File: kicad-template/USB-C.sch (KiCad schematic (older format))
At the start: 4 parts

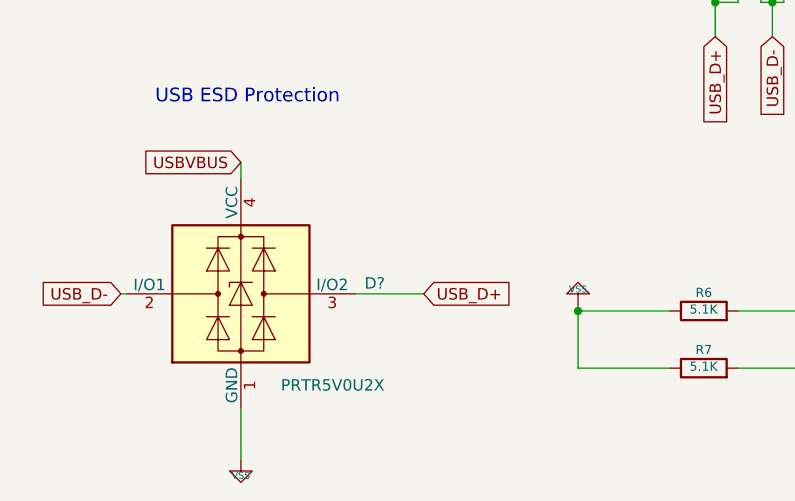
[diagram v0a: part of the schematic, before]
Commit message: working on adding support for jlcpcb small batch assembly
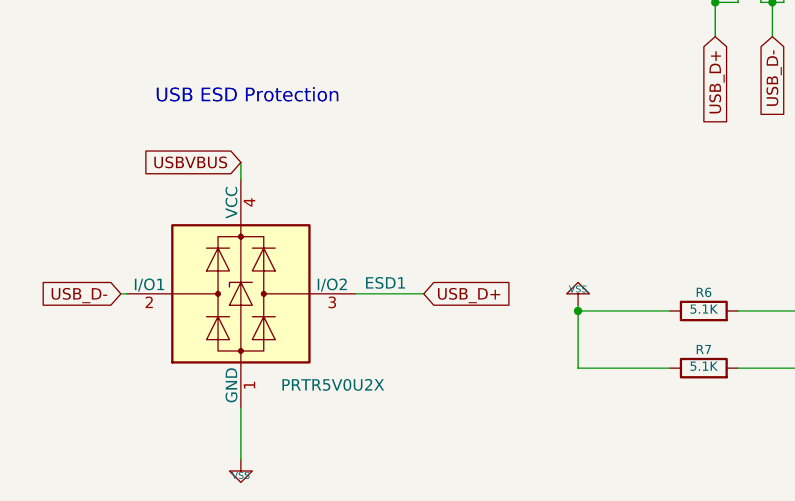
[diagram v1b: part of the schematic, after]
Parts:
- ESD1: LCSC (none) -> C12333
- R7: DigiKey RR08P5.1KDTR-ND -> YAG1696TR-ND; LCSC (none) -> C122969; MPN RR0816P-512-D -> RT0603BRD075K1L; Manufacturer Susumu -> Yaego
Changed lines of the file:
@@
 AR Path="/5B90A59F/5B5FAE80" Ref="R7"  Part="1"
 AR Path="/5D950BDF/5B5FAE80" Ref="R?"  Part="1"
-F 0 "R?" V 3980 5350 40  0000 C CNN
+F 0 "R7" V 3980 5350 40  0000 C CNN
 F 1 "5.1K" V 3907 5351 40  0000 C CNN
 F 2 "Resistor_SMD:R_0603_1608Metric" V 3830 5350 30  0001 C CNN
-F 3 "http://www.susumu.co.jp/common/pdf/n_catalog_partition05_en.pdf" H 3900 5350 30  0001 C CNN
-F 4 "RR0816P-512-D" V 3900 5350 50  0001 C CNN "MPN"
+F 3 "" H 3900 5350 30  0001 C CNN
+F 4 "RT0603BRD075K1L" V 3900 5350 50  0001 C CNN "MPN"
 F 5 "RES SMD 5.1K OHM 0.5% 1/16W 0603" H -5700 275 50  0001 C CNN "Description"
-F 6 "RR08P5.1KDTR-ND" H -5700 275 50  0001 C CNN "DigiKey"
-F 7 "Susumu" H -5700 275 50  0001 C CNN "Manufacturer"
+F 6 "YAG1696TR-ND" H -5700 275 50  0001 C CNN "DigiKey"
+F 7 "Yaego" H -5700 275 50  0001 C CNN "Manufacturer"
 F 8 "RT0603BRD075K1L	" H 0   0   50  0001 C CNN "Seeed Part Num"
+F 9 "C122969" V 3900 5350 50  0001 C CNN "LCSC"
 	1    3900 5350
 	0    -1   -1   0
@@
 AR Path="/5B90A59F/5B5FB101" Ref="R6"  Part="1"
 AR Path="/5D950BDF/5B5FB101" Ref="R?"  Part="1"
-F 0 "R?" V 3980 5100 40  0000 C CNN
+F 0 "R6" V 3980 5100 40  0000 C CNN
 F 1 "5.1K" V 3907 5101 40  0000 C CNN
 F 2 "Resistor_SMD:R_0603_1608Metric" V 3830 5100 30  0001 C CNN
@@
 AR Path="/5B90A59F/5B5FB0C4" Ref="USB1"  Part="1"
 AR Path="/5D950BDF/5B5FB0C4" Ref="USB?"  Part="1"
-F 0 "USB?" V 3809 4329 50  0000 L CNN
+F 0 "USB1" V 3809 4329 50  0000 L CNN
 F 1 "USB_C_Receptacle" V 3900 4329 50  0000 L CNN
 F 2 "Keyboardio:USB-TYPE-C-MIDMOUNT" H 3900 2900 50  0001 C CNN
@@
 AR Path="/5B90A59F/5CA6A217" Ref="ESD1"  Part="1"
 AR Path="/5D950BDF/5CA6A217" Ref="D?"  Part="1"
-F 0 "D?" H 2416 5071 50  0000 L CNN
+F 0 "ESD1" H 2416 5071 50  0000 L CNN
 F 1 "PRTR5V0U2X" H 2050 4625 50  0000 L CNN
 F 2 "Keyboardio:PRTR5V0U2X" H 1935 5025 50  0001 C CNN
@@
 F 7 "Nexperia" H -2925 -125 50  0001 C CNN "Manufacturer"
 F 8 "PRTR5V0U2X,215	" H 0   0   50  0001 C CNN "Seeed Part Num"
+F 9 "C12333" H 1875 5025 50  0001 C CNN "LCSC"
 	1    1875 5025
 	1    0    0    -1

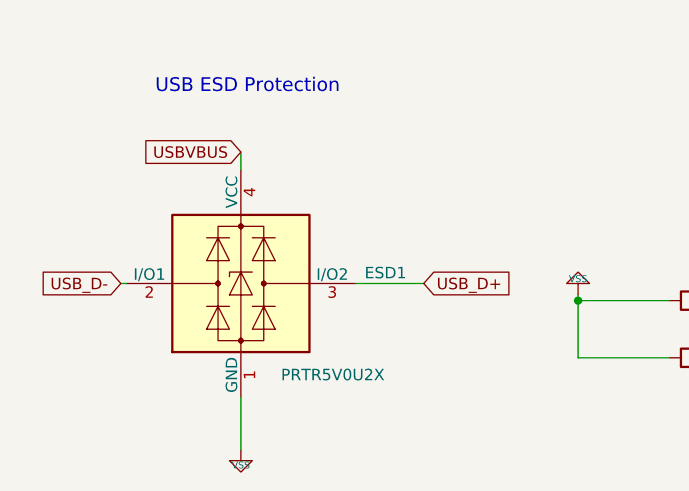
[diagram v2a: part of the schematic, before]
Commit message: Trying to get back to Kicad 5.1 compat and fix USB routing
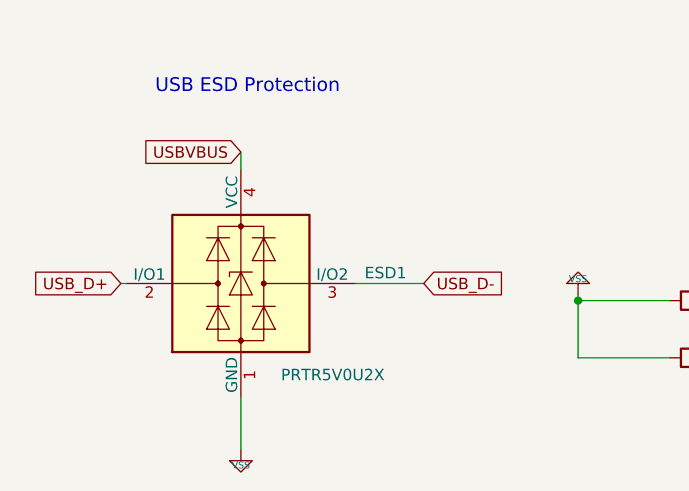
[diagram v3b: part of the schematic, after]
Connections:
- net USB_D+: now also ESD1.2 (I/O1); no longer ESD1.3 (I/O2)
- net USB_D-: now also ESD1.3 (I/O2); no longer ESD1.2 (I/O1)
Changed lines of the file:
@@
-EESchema Schematic File Version 5
+EESchema Schematic File Version 4
 LIBS:kicad-template-cache
 EELAYER 30 0
@@
 Comment3 ""
 Comment4 ""
-Comment5 ""
-Comment6 ""
-Comment7 ""
-Comment8 ""
-Comment9 ""
 $EndDescr
 $Comp
@@
 U 1 1 5CA6F860
 P 1850 2800
-AR Path="/5B90A59F/5CA6F860" Ref="#FLG?"  Part="1"
-AR Path="/5D950BDF/5CA6F860" Ref="#FLG?"  Part="1"
 F 0 "#FLG?" H 1850 2895 50  0001 C CNN
 F 1 "PWR_FLAG" V 1850 3100 50  0000 C CNN
@@
 U 1 1 5B5FAE80
 P 3900 5350
-AR Path="/5B90A59F/5B5FAE80" Ref="R7"  Part="1"
-AR Path="/5D950BDF/5B5FAE80" Ref="R7"  Part="1"
 F 0 "R7" V 3980 5350 40  0000 C CNN
 F 1 "5.1K" V 3907 5351 40  0000 C CNN
@@
 U 1 1 5B5FB101
 P 3900 5100
-AR Path="/5B90A59F/5B5FB101" Ref="R6"  Part="1"
-AR Path="/5D950BDF/5B5FB101" Ref="R6"  Part="1"
 F 0 "R6" V 3980 5100 40  0000 C CNN
 F 1 "5.1K" V 3907 5101 40  0000 C CNN
@@
 U 1 1 5B5FB0C4
 P 3750 2900
-AR Path="/5B90A59F/5B5FB0C4" Ref="USB1"  Part="1"
-AR Path="/5D950BDF/5B5FB0C4" Ref="USB1"  Part="1"
 F 0 "USB1" V 3809 4329 50  0000 L CNN
 F 1 "USB_C_Receptacle" V 3900 4329 50  0000 L CNN
@@
 U 1 1 5CA6F862
 P 5175 3550
-AR Path="/5B90A59F/5CA6F862" Ref="#FLG?"  Part="1"
-AR Path="/5D950BDF/5CA6F862" Ref="#FLG?"  Part="1"
 F 0 "#FLG?" H 5175 3625 50  0001 C CNN
 F 1 "PWR_FLAG" H 5175 3723 50  0000 C CNN
@@
 U 1 1 5CA6A217
 P 1875 5025
-AR Path="/5CA54797/5CA6A217" Ref="ESD1"  Part="1"
-AR Path="/5B90A59E/5CA5B11A/5CA6A217" Ref="ESD1"  Part="1"
-AR Path="/5B90A59F/5CA5B290/5CA6A217" Ref="ESD1"  Part="1"
-AR Path="/5B90A59E/5CA6A217" Ref="ESD1"  Part="1"
-AR Path="/5D950BDF/5CA6A217" Ref="ESD1"  Part="1"
 F 0 "ESD1" H 2416 5071 50  0000 L CNN
 F 1 "PRTR5V0U2X" H 2050 4625 50  0000 L CNN
@@
 U 1 1 5CA6A220
 P 1875 5750
-AR Path="/5CA54797/5CA6A220" Ref="#PWR?"  Part="1"
-AR Path="/5B90A59E/5CA5B11A/5CA6A220" Ref="#PWR?"  Part="1"
-AR Path="/5B90A59F/5CA5B290/5CA6A220" Ref="#PWR?"  Part="1"
-AR Path="/5B90A59E/5CA6A220" Ref="#PWR?"  Part="1"
-AR Path="/5B90A59F/5CA6A220" Ref="#PWR?"  Part="1"
 F 0 "#PWR?" H 1875 5750 30  0001 C CNN
 F 1 "VSS" H 1875 5680 30  0000 C CNN
@@
 	1875 5525 1875 5750
 Text GLabel 2675 5025 2    50   Input ~ 0
-USB_D+
+USB_D-
 Text GLabel 1875 4450 0    50   Input ~ 0
 USBVBUS
 Text GLabel 1350 5025 0    50   Input ~ 0
-USB_D-
+USB_D+
 Text Notes 7525 2050 0    197  ~ 39
 USB Support Circuitry
